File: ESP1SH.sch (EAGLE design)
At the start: 28 parts, among them J1 Digital_0_7, J2 Analog, J3 Digital_8_13, J4 Power, J5 BT-TX, J6 Digital_0_7, J7 BT-RX, J8 ICSP, J9 ESP01, Q1 RJU003N03 N-MOSFET, Q2 RJU003N03 N-MOSFET

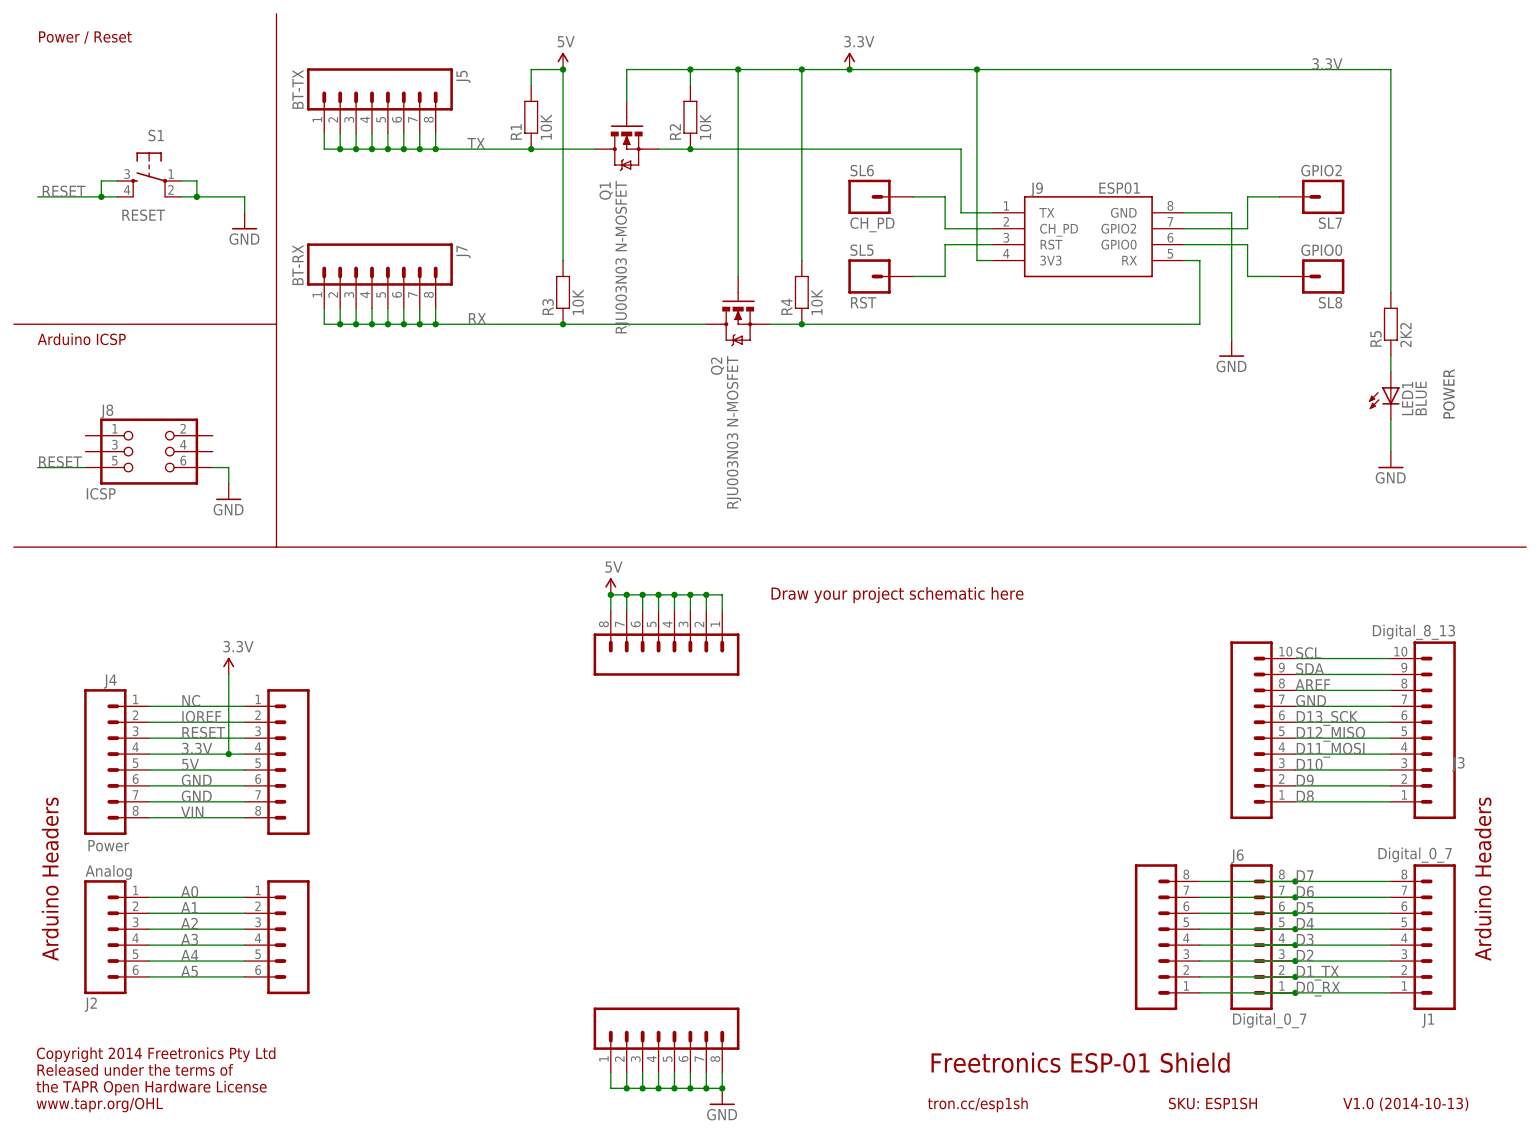
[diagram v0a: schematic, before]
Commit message: Added onboard voltage regulator for v1.1 release
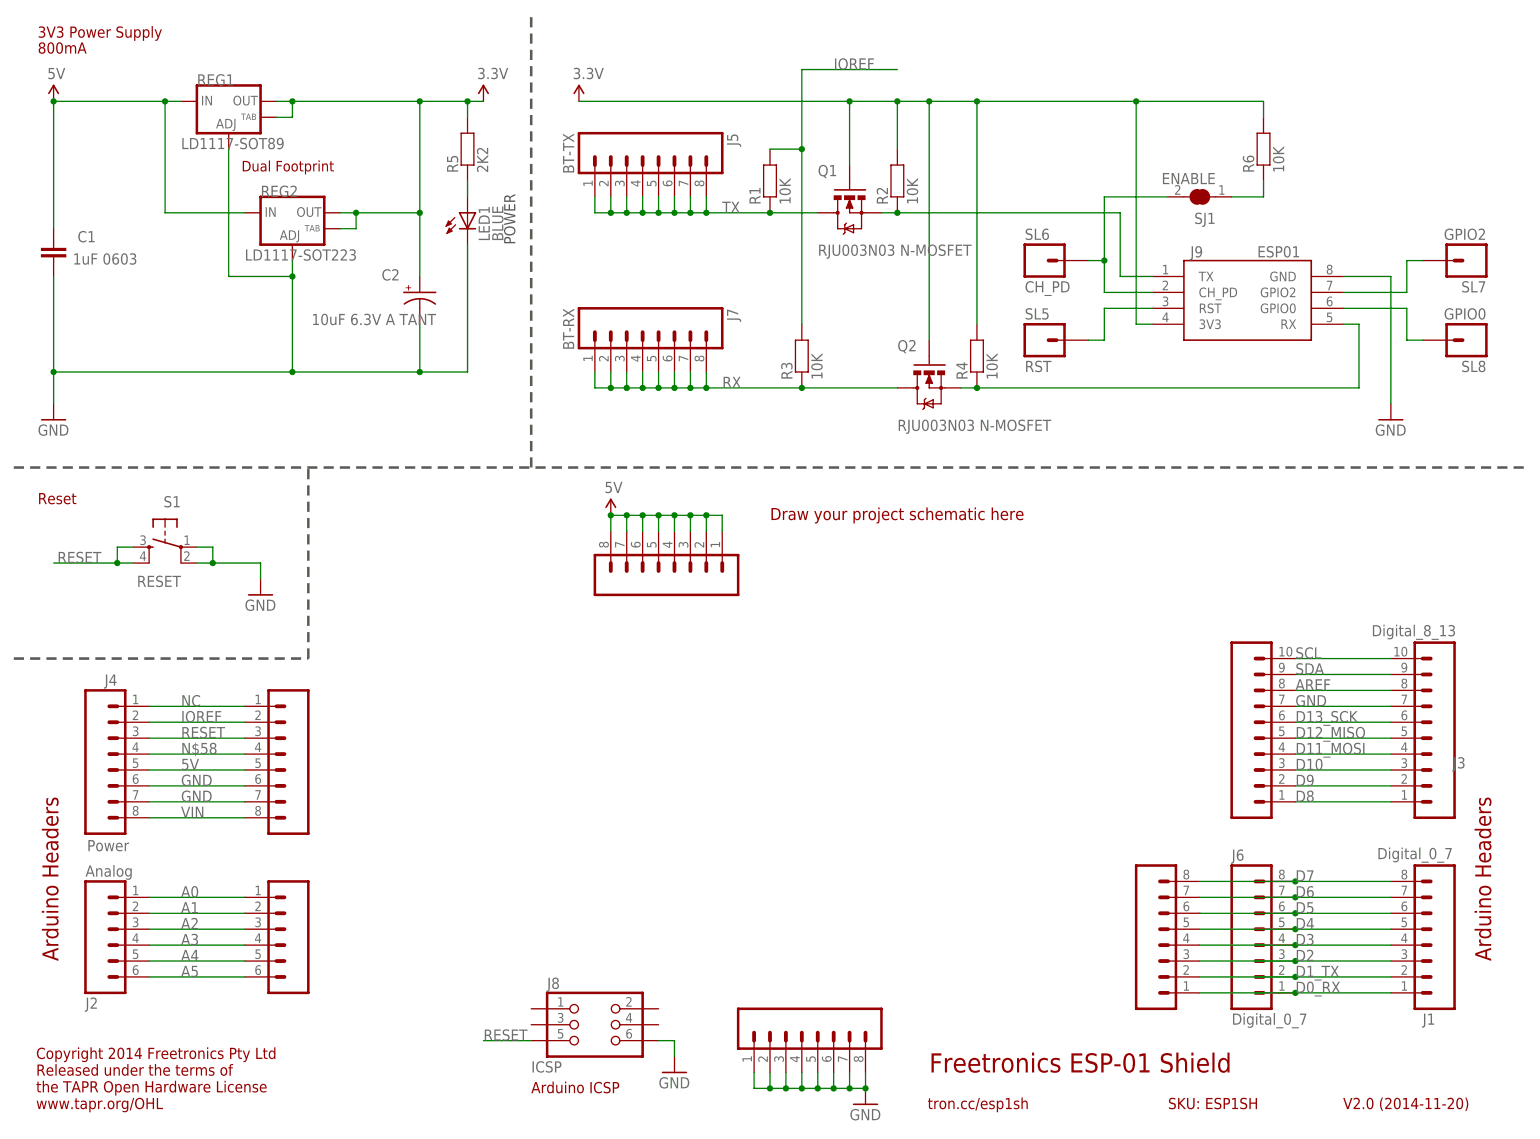
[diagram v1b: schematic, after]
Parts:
- added C1: 1uF 0603, freetronics:CAP0603
- added C2: 10uF 6.3V A TANT, freetronics:CAP_POL1206
- added R6: 10K, freetronics-jon:RESISTOR0603
- added REG1: LD1117-SOT89, freetronics:V_REG_LM1117SOT89
- added REG2: LD1117-SOT223, freetronics:V_REG_LM1117SOT223
- added SJ1: ENABLE, freetronics-jon:SJCN
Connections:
- new net N$58: J4.4, SL4.4
- new net N$60: R6.1, SJ1.1
- net 3.3V: now also C2.+, R6.2, REG1.OUT, REG1.OUT@1, REG2.OUT, REG2.OUT@1; no longer J4.4, SL4.4
- net 5V: now also C1.1, REG1.IN, REG2.IN; no longer R1.2, R3.2
- net GND: now also C1.2, C2.-, REG1.ADJ, REG2.ADJ
- net IOREF: now also R1.2, R3.2
- net N$4: now also SJ1.2
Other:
- note added: "3V3 Power Supply"
- note added: "800mA"
- note added: "Dual Footprint"
- note added: "Reset"
- note added: "V2.0 (2014-11-20)"
- note removed: "Power / Reset"
- note removed: "V1.0 (2014-10-13)"
- moved on the sheet: J5, J7, J8, J9, LED1, Q1, Q2, R1, R2, R3, R4, R5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

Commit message: Added REFLASH button connected to CH_PD
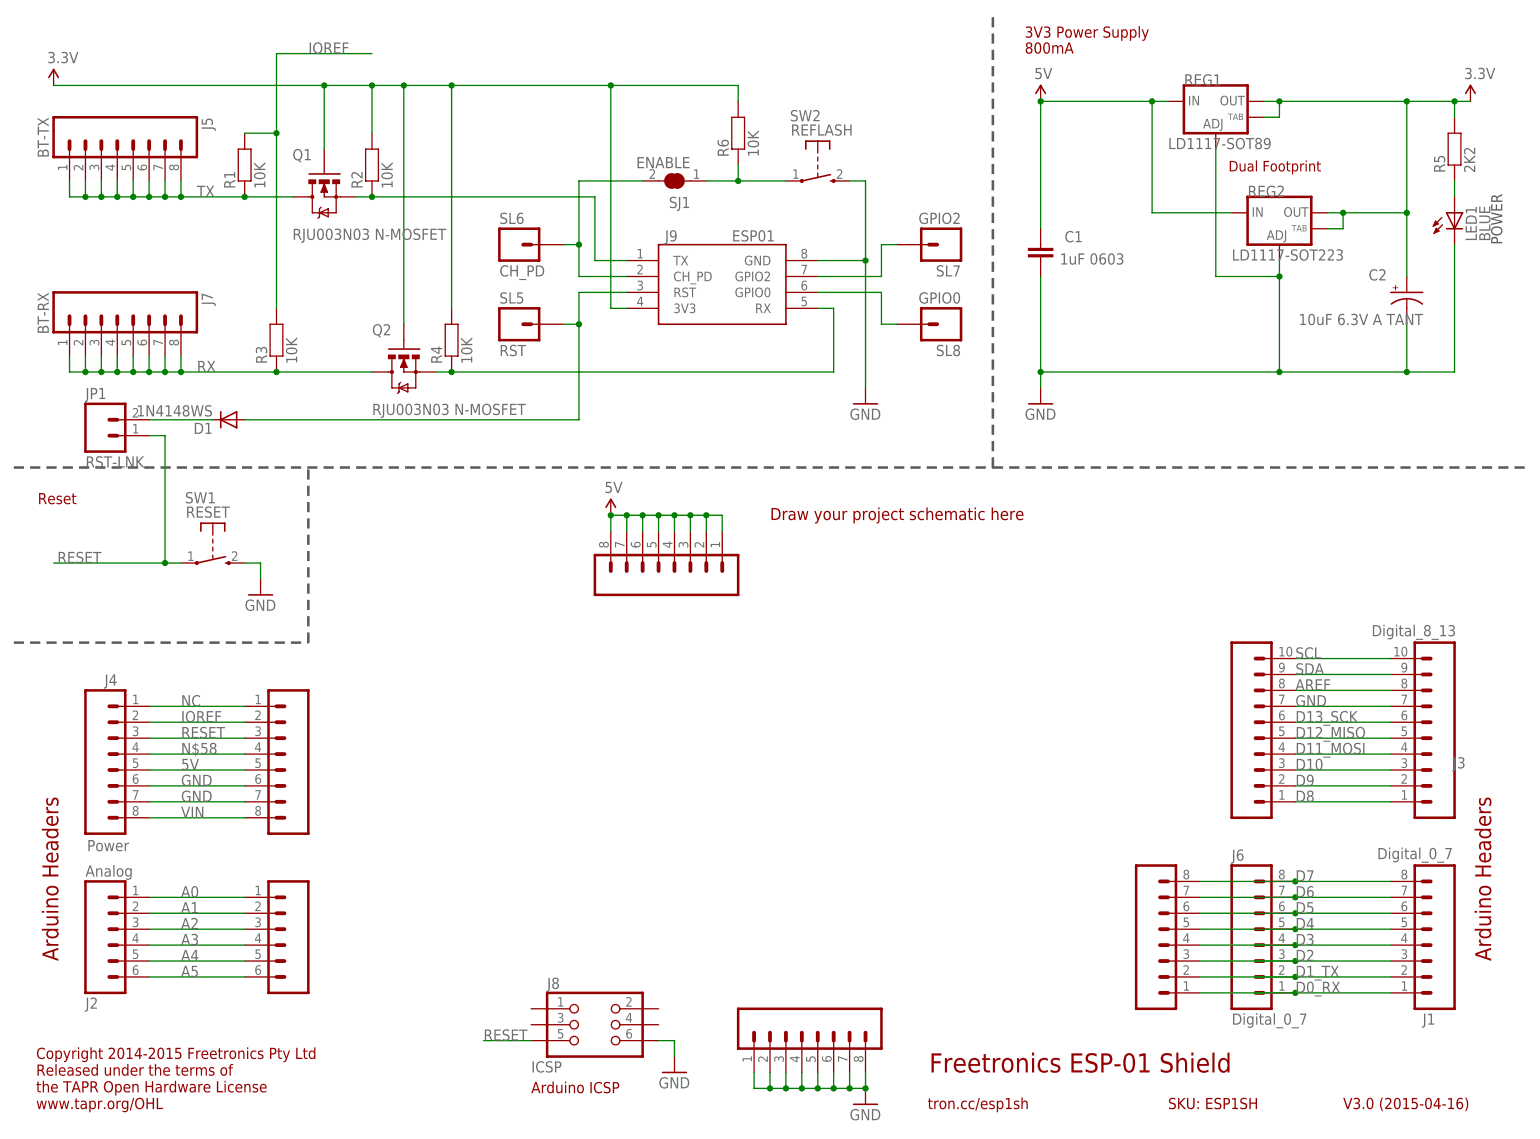
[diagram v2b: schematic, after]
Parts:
- removed S1: RESET, freetronics-original:TAC_SWITCHSMD
- added D1: 1N4148WS, freetronics-original:DIODESOD
- added JP1: RST-LNK, freetronics-original:M02PTH
- added SW1: RESET, freetronics-master-v1:TAC_SWITCH_2PIN
- added SW2: REFLASH, freetronics-master-v1:TAC_SWITCH_2PIN
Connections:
- new net N$61: D1.C, JP1.2
- net GND: now also SW1.S, SW2.S; no longer S1.1, S1.2
- net N$3: now also D1.A
- net N$60: now also SW2.P
- net RESET: now also JP1.1, SW1.P; no longer S1.3, S1.4
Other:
- note added: "Copyright 2014-2015 Freetronics Pty Ltd Released under the terms of the TAPR Open Hardware License www.tapr.org/OHL"
- note added: "V3.0 (2015-04-16)"
- note removed: "Copyright 2014 Freetronics Pty Ltd Released under the terms of the TAPR Open Hardware License www.tapr.org/OHL"
- note removed: "V2.0 (2014-11-20)"
- moved on the sheet: C1, C2, J5, J7, J9, LED1, Q1, Q2, R1, R2, R3, R4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

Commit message: Changed REFLASH button from CH_PD to GPIO0
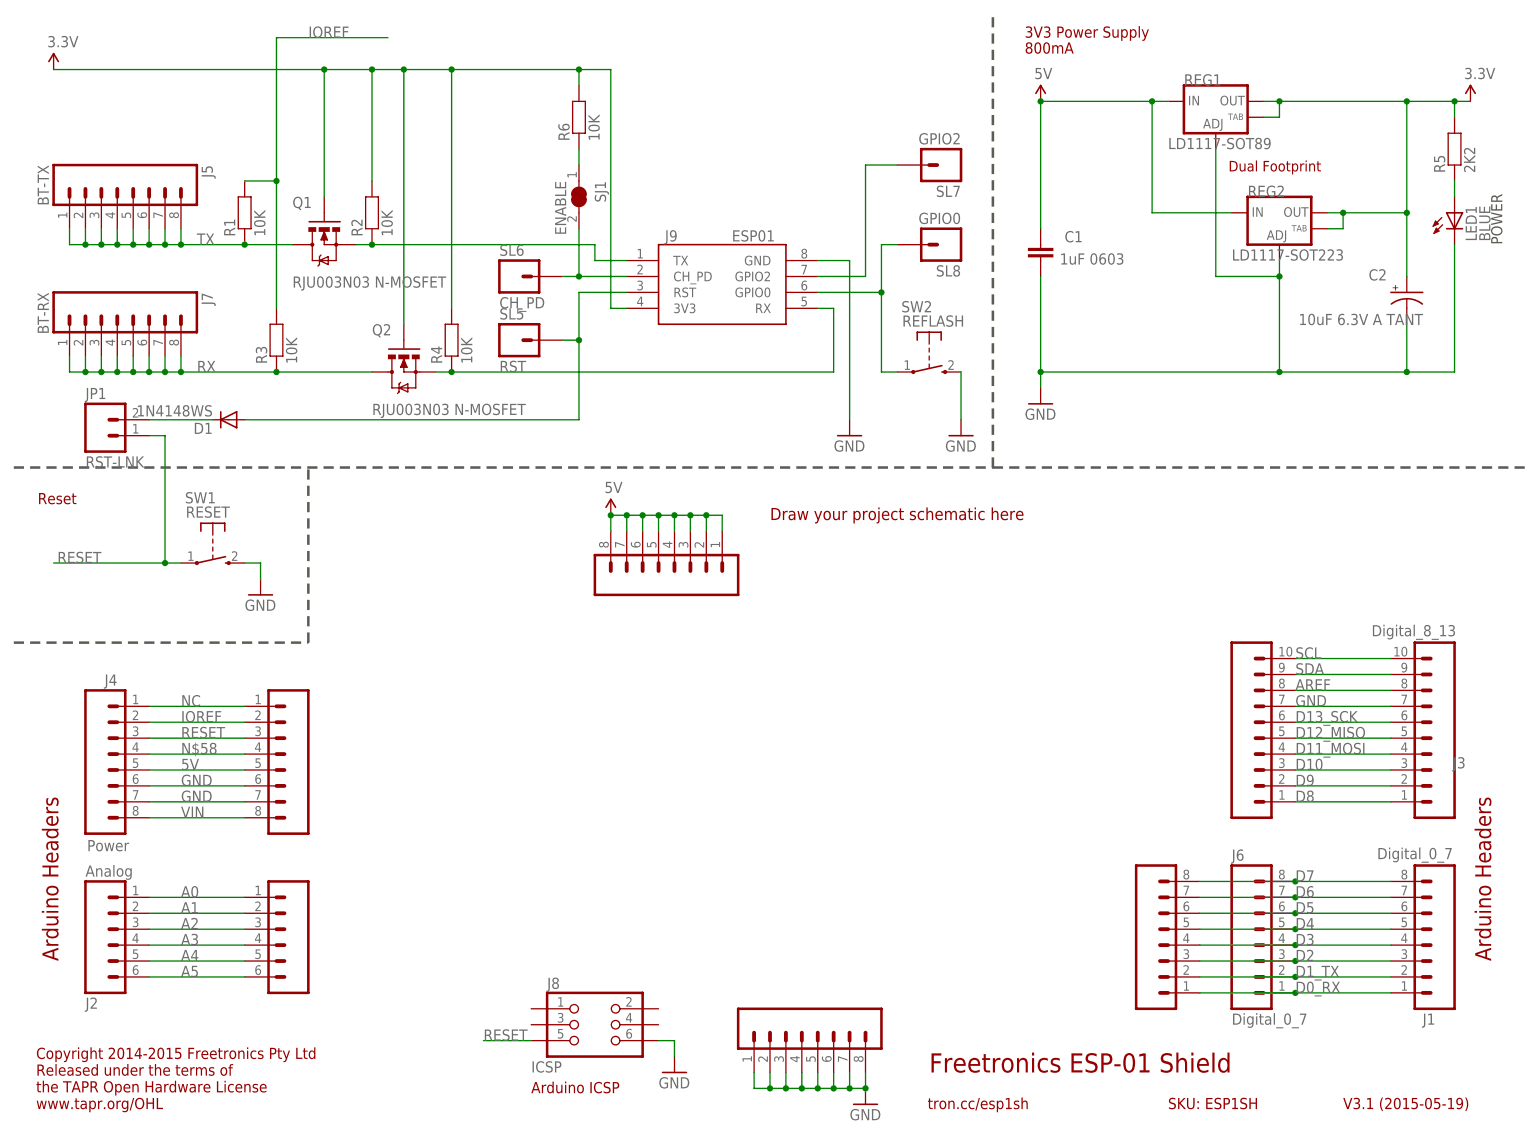
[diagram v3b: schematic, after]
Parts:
- SW1, SW2: device freetronics-master-v1:TAC_SWITCH_2PIN -> freetronics-jon:TAC_SWITCH_2PIN
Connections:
- net N$1: now also SW2.P
- net N$60: no longer SW2.P
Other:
- note added: "V3.1 (2015-05-19)"
- note removed: "V3.0 (2015-04-16)"
- moved on the sheet: J5, Q1, R1, R2, R6, SJ1, SL5, SL6, SL7, SL8, SW2
